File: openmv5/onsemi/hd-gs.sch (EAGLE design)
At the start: 58 parts, among them IC1 AP0202AT2L00XPGA0, IC2 MIC5365-2.8YC5-TR, IC3 TLV62568PDDCR, J1 DF12-36-DS, J2 DF12-36-DP, M1 9774030151R, M2 9774030151R, Q1 PMXB120EPEZ

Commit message: Add more cameras
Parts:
- removed J2: DF12-36-DP, DF12NB(3.0)-36DP-0.5V(51):DF12-36-DP
- removed L7: 100, 0402:INDUCTOR_0402
- removed M1, M2: 9774030151R, 9774030151R:9774030151R
- removed R5: 100K, rcl:R-US_R0402
- removed R6: 10K, rcl:R-US_R0402
- added C30, C31, C33, C34: 4.7uF, 0402:CAP_0402
- added C32, C35, C36: 22uF, SparkFun-Capacitors:22UF-0805-6.3V-20%
- added H1: LENSMOUNT20MM, lensmount:LENSMOUNT20MM
- C1, C13: value 0.22uF -> 4.7uF; device rcl:C-EUC0201 -> 0402:CAP_0402; MPN GRM033R60J224ME15D -> JMK105BBJ475MV-F
- C12: value 6.8pF -> 0.22uF; device 0402:CAP_0402 -> rcl:C-EUC0201; MPN GRM1555C1H6R8DA01D -> GRM033R60J224ME15D
- C14, C16, C18, C19, C20, C22, C23: value 4.7uF -> 0.22uF; device 0402:CAP_0402 -> rcl:C-EUC0201; MPN JMK105BBJ475MV-F -> GRM033R60J224ME15D
- C15: value 4.7uF -> 22uF; device 0402:CAP_0402 -> SparkFun-Capacitors:22UF-0805-6.3V-20%; MPN JMK105BBJ475MV-F -> CL21A226MQQNNNE
- C17, C24, C25, C26: value 22uF -> 0.22uF; device SparkFun-Capacitors:22UF-0805-6.3V-20% -> rcl:C-EUC0201; MPN CL21A226MQQNNNE -> GRM033R60J224ME15D
- C2: value 0.22uF -> 22uF; device rcl:C-EUC0201 -> SparkFun-Capacitors:22UF-0805-6.3V-20%; MPN GRM033R60J224ME15D -> CL21A226MQQNNNE
- C21: value 4.7uF -> 6.8pF; MPN JMK105BBJ475MV-F -> GRM1555C1H6R8DA01D
- C27, C29: value 22uF -> 4.7uF; device SparkFun-Capacitors:22UF-0805-6.3V-20% -> 0402:CAP_0402; MPN CL21A226MQQNNNE -> JMK105BBJ475MV-F
- IC1: value AP0202AT2L00XPGA0 -> TLV62568PDDCR; device AP0202AT2L00XPGA0:AP0202AT2L00XPGA0 -> TLV62568PDDCR:TLV62568PDDCR; MPN AP0202AT2L00XPGA0-DR -> TLV62568PDDCR
- IC2: value MIC5365-2.8YC5-TR -> AR0144CSSC20SUKA0; device MIC5365-2.8YC5-TR:MIC5365-2.8YC5-TR -> AR0144CSSC20SUKA0:AR0144CSSC20SUKA0; MPN MIC5365-2.8YC5-TR -> AR0144CSSC20SUKA0-CRBR
- IC3: value TLV62568PDDCR -> MIC5365-2.8YC5-TR; device TLV62568PDDCR:TLV62568PDDCR -> MIC5365-2.8YC5-TR:MIC5365-2.8YC5-TR; MPN TLV62568PDDCR -> MIC5365-2.8YC5-TR
- J1: value DF12-36-DS -> DF12-36-DP; device DF12-36-DS:DF12-36-DS -> DF12NB(3.0)-36DP-0.5V(51):DF12-36-DP; MPN DF12NB-36DS-0.5V(51) -> DF12NB(3.0)-36DP-0.5V(51)
- L1: value MAKK2016T2R2M -> 100; device MAKK2016T2R2M:MAKK2016T2R2M -> 0402:INDUCTOR_0402; MPN MAKK2016T2R2M -> MFBM1V1005-101-R
- L3: value 100 -> MAKK2016T2R2M; device 0402:INDUCTOR_0402 -> MAKK2016T2R2M:MAKK2016T2R2M; MPN MFBM1V1005-101-R -> MAKK2016T2R2M
- R1, R2: value 1.5K -> 100K; MPN RC0402FR-131K5L -> AC0402FR-07100KL
- R3: value 100K -> 10K; MPN AC0402FR-07100KL -> AC0402FR-1310KL
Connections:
- net SENSOR_D12 renamed DCMI_D12
- net SENSOS_D13 renamed DCMI_D13
- removed net DCMI_MISO: J1.15, J2.15
- removed net DCMI_MOSI: J1.17, J2.17
- removed net DCMI_SCLK: J1.13, J2.13
- removed net DCMI_SSEL: J1.11, J2.11
- removed net SENSOR_CLK: IC1.EXT_CLK_OUT, J1.12
- removed net SENSOR_D0: IC1.DIN_0, J1.3
- removed net SENSOR_D1: IC1.DIN_1, J1.1
- removed net SENSOR_D10: IC1.DIN_10, J1.24
- removed net SENSOR_D11: IC1.DIN_11, J1.22
- removed net SENSOR_D2: IC1.DIN_2, J1.9
- removed net SENSOR_D3: IC1.DIN_3, J1.7
- removed net SENSOR_D4: IC1.DIN_4, J1.31
- removed net SENSOR_D5: IC1.DIN_5, J1.29
- removed net SENSOR_D6: IC1.DIN_6, J1.35
- removed net SENSOR_D7: IC1.DIN_7, J1.28
- removed net SENSOR_D8: IC1.DIN_8, J1.26
- removed net SENSOR_D9: IC1.DIN_9, J1.33
- removed net SENSOR_FSIN: IC1.TRIGGER_OUT/GPIO_0, J1.23
- removed net SENSOR_HSYNC: IC1.LV_IN, J1.18
- removed net SENSOR_PCLK: IC1.PIXCLK_IN, J1.14
- removed net SENSOR_RST: IC1.RESET_N_OUT, J1.21
- removed net SENSOR_SCL: IC1.M_SCLK, J1.32, R1.1
- removed net SENSOR_SDA: IC1.M_SDATA, J1.34, R2.1
- removed net SENSOR_VSYNC: IC1.FV_IN, J1.16
- removed net VDDIO_H: C13.2, C19.2, C2.2, C25.2, C3.2, C4.2, IC1.EXT_REG, IC1.SADDR, IC1.VDDIO_H0, IC1.VDDIO_H1, IC1.VDDIO_H2, IC1.VDD_REG, L3.P$1
- removed net VDDIO_OTPM: C10.2, C18.2, C24.2, IC1.VDDIO_OTPM, L2.P$1
- removed net VDDIO_S: C1.2, C20.2, C26.2, IC1.VDDIO_S, L4.P$1
- removed net VDD_PLL: C22.2, C28.2, C5.2, IC1.VDD_PLL, L6.P$1
- new net DCMI_D10: IC2.DOUT10, J1.24
- new net DCMI_D11: IC2.DOUT11, J1.22
- new net DCMI_D8: IC2.DOUT8, J1.26
- new net DCMI_D9: IC2.DOUT9, J1.33
- new net SPI_MISO: J1.15
- new net SPI_MOSI: J1.17
- new net SPI_SCLK: J1.13
- new net SPI_SSEL: J1.11
- new net VAA: C3.1, C31.2, C32.2, C4.1, C5.1, C6.1, C7.1, C8.1, IC2.VAA0, IC2.VAA1, IC2.VAA2, IC2.VAA3, IC2.VAA4, IC2.VAA5, L4.P$1
- new net VAA_PIX: C20.1, C33.2, C35.2, IC2.VAA_PIX, L5.P$1
- new net VDDIO: C22.1, C23.1, C24.1, C25.1, C26.1, C34.2, C36.2, IC2.VDDIO0, IC2.VDDIO1, IC2.VDDIO2, IC2.VDDIO3, IC2.VDDIO4, L6.P$1
- net DCMI_CLK: now also IC2.EXTCLK, J1.12; no longer IC1.EXTCLK, J2.12
- net DCMI_D0: now also IC2.DOUT0, J1.3; no longer IC1.DOUT_16, J2.31
- net DCMI_D1: now also IC2.DOUT1, J1.1; no longer IC1.DOUT_17, J2.29
- net DCMI_D2: now also IC2.DOUT2, J1.9; no longer IC1.DOUT_18, J2.35
- net DCMI_D3: now also IC2.DOUT3, J1.7; no longer IC1.DOUT_19, J2.28
- net DCMI_D4: now also IC2.DOUT4, J1.31; no longer IC1.DOUT_20, J2.26
- net DCMI_D5: now also IC2.DOUT5, J1.29; no longer IC1.DOUT_21, J2.33
- net DCMI_D6: now also IC2.DOUT6, J1.35; no longer IC1.DOUT_22, J2.24
- net DCMI_D7: now also IC2.DOUT7, J1.28; no longer IC1.DOUT_23, J2.22
- net DCMI_FSIN: now also IC2.TRIGGER, J1.23; no longer IC1.FRAME_SYNC, J2.23
- net DCMI_HSYNC: now also IC2.LINE_VALID, J1.18; no longer IC1.LV_OUT, J2.18
- net DCMI_PCLK: now also IC2.PIXCLK, J1.14; no longer IC1.PIXCLK_OUT, J2.14
- net DCMI_PWDN: no longer IC1.STANDBY, J2.25
- net DCMI_PWDN_INT: now also IC3.EN, R4.1; no longer IC2.EN, R5.1
- net DCMI_RST: now also J1.21, R3.2; no longer J2.21, R6.2
- net DCMI_SCL: now also IC2.SCLK, J1.32; no longer IC1.SCLK, J2.32
- net DCMI_SDA: now also IC2.SDATA, J1.34; no longer IC1.SDATA, J2.34
- net DCMI_VSYNC: now also IC2.FRAME_VALID, J1.16; no longer IC1.FV_OUT, J2.16
- net FB: now also C21.2, IC1.FB, R1.1, R2.1; no longer C12.2, IC3.FB, R3.1, R4.1
- net GND: now also C10.2, C11.2, C12.2, C14.2, C16.2, C17.2, C18.2, C19.2, C20.2, C22.2, C23.2, C24.2, C25.2, C26.2, C3.2, C30.1, C31.1, C32.1, C33.1, C34.1, C35.1, C36.1, C4.2, C5.2, C6.2, C7.2, C8.2, C9.2, IC1.GND, IC2.AGND0, IC2.AGND1, IC2.AGND2, IC2.AGND3, IC2.AGND4, IC2.DGND0, IC2.DGND1, IC2.DGND2, IC2.DGND3, IC2.DGND4, IC2.DGND5, IC2.DGND6, IC2.DGND7, IC2.DGND8, IC2.DGND9, IC2.OE_N, IC2.SADDR, IC2.TEST, R2.2; no longer C10.1, C11.1, C14.1, C16.1, C17.1, C18.1, C19.1, C20.1, C21.1, C22.1, C23.1, C24.1, C25.1, C26.1, C3.1, C4.1, C5.1, C6.1, C7.1, C8.1, C9.1, IC1.DGND, IC1.ENDLO, IC1.GND0, IC1.GND1, IC1.GND2, IC1.GND3, IC1.GND4, IC1.GND5, IC1.GND6, IC1.GND7, IC1.HISPI0N, IC1.HISPI0P, IC1.HISPI1N, IC1.HISPI1P, IC1.HISPICN, IC1.HISPICP, IC1.RESERVED_0, IC1.RESERVED_1, IC1.SPI_SDI, IC1.TEST, IC2.GND, J2.19, J2.27, J2.5, R5.2
- net RESET_N: now also IC1.PG, IC2.RESET_N, R3.1; no longer IC1.RESET_N, IC3.PG, R6.1
- net SW: now also IC1.SW, L3.2; no longer IC3.SW, L1.2
- net VCC: now also C27.2, IC1.VIN; no longer C15.2, C16.2, IC2.VIN, IC3.VIN, J2.10, J2.2, J2.20, J2.30, J2.36, L2.P$2, L3.P$2, Q1.S, R1.2, R2.2
- net VDD: now also C1.2, C10.1, C11.1, C12.1, C14.1, C16.1, C17.1, C18.1, C19.1, C2.2, IC2.VDD0, IC2.VDD1, IC2.VDD2, IC2.VDD3, IC2.VDD4, IC2.VDD5, IC2.VDD6, IC2.VDD7, L1.P$1; no longer C23.2, C29.2, C6.2, C7.2, C8.2, C9.2, IC1.VDD0, IC1.VDD1, IC1.VDD2, IC1.VDD3, L7.P$1
- net VDDA: now also C30.2, IC3.VIN, Q1.S; no longer J2.4
- net VDDIO_REG: now also C29.2, IC1.EN, IC3.VOUT, L6.P$2; no longer C14.2, IC2.VOUT, IC3.EN
- net VDD_PHY: now also C13.2, C15.2, C9.1, IC2.VDD_PHY, L2.P$1; no longer C11.2, C21.2, C27.2, IC1.VDD_PHY, L5.P$1
- net VDD_REG: now also C21.1, C28.2, L1.P$2, L2.P$2, L3.1, R1.2; no longer C12.1, C17.2, L1.1, L6.P$2, L7.P$2, R3.2
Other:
- note added: "Camera Sensor"
- note added: "Connector"
- note removed: "Host Connector"
- note removed: "ISP"
- note removed: "SENSOR CONNECTOR"
- moved on the sheet: C1, C10, C11, C12, C13, C14, C15, C16, C17, C18, C19, C2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

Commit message: Finish out new onsemi cameras
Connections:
- removed net DCMI_D12: J1.8
- removed net DCMI_D13: J1.6
- net GND: now also J1.6, J1.8
- net SPI_MISO: now also IC2.FLASH
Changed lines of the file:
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@@
 <wire x1="17.78" y1="220.98" x2="43.18" y2="220.98" width="0.1524" layer="91"/>
+</segment>
+<segment>
+<wire x1="381" y1="228.6" x2="411.48" y2="228.6" width="0.1524" layer="91"/>
+<label x="386.08" y="228.6" size="1.778" layer="95"/>
+<pinref part="J1" gate="G$1" pin="6"/>
+</segment>
+<segment>
+<wire x1="381" y1="226.06" x2="411.48" y2="226.06" width="0.1524" layer="91"/>
+<label x="386.08" y="226.06" size="1.778" layer="95"/>
+<pinref part="J1" gate="G$1" pin="8"/>
 </segment>
 </net>
@@
 <pinref part="J1" gate="G$1" pin="15"/>
 </segment>
+<segment>
+<pinref part="IC2" gate="G$1" pin="FLASH"/>
+<wire x1="43.18" y1="200.66" x2="22.86" y2="200.66" width="0.1524" layer="91"/>
+<label x="25.4" y="200.66" size="1.778" layer="95"/>
+</segment>
 </net>
 <net name="SPI_MOSI" class="4">
@@
 </segment>
 </net>
-<net name="DCMI_D13" class="4">
-<segment>
-<wire x1="381" y1="228.6" x2="411.48" y2="228.6" width="0.1524" layer="91"/>
-<label x="386.08" y="228.6" size="1.778" layer="95"/>
-<pinref part="J1" gate="G$1" pin="6"/>
-</segment>
-</net>
-<net name="DCMI_D12" class="4">
-<segment>
-<wire x1="381" y1="226.06" x2="411.48" y2="226.06" width="0.1524" layer="91"/>
-<label x="386.08" y="226.06" size="1.778" layer="95"/>
-<pinref part="J1" gate="G$1" pin="8"/>
-</segment>
-</net>

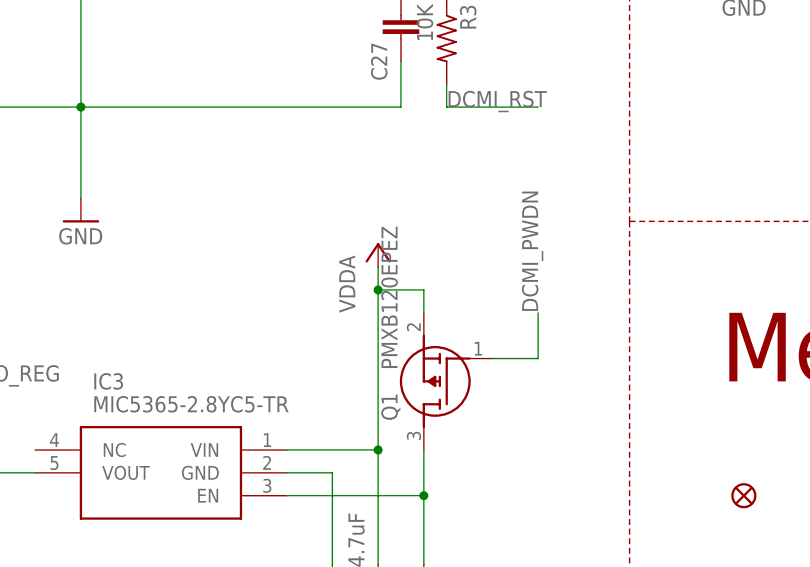
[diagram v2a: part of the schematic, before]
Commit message: Update camera modules to use different non-flippable pmosfet
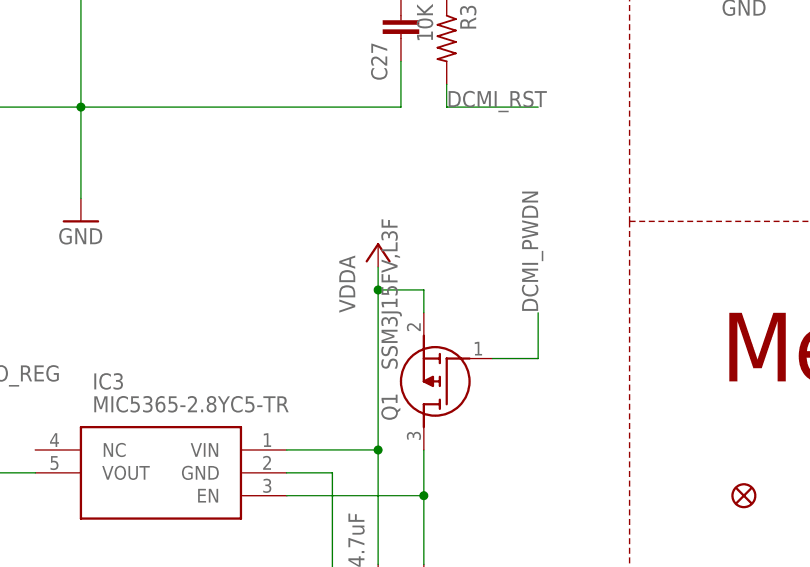
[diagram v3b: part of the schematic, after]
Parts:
- Q1: value PMXB120EPEZ -> SSM3J15FV,L3F; device PMXB120EPEZ:PMXB120EPEZ -> SSM3J15FV_L3F:SSM3J15FV,L3F; MPN PMXB120EPEZ -> SSM3J15FV,L3F
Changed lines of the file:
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@@
 </part>
 <part name="GND11" library="supply" deviceset="GND" device=""/>
-<part name="Q1" library="PMXB120EPEZ" deviceset="PMXB120EPEZ" device="">
-<attribute name="MPN" value="PMXB120EPEZ"/>
+<part name="Q1" library="SSM3J15FV_L3F" deviceset="SSM3J15FV,L3F" device="">
+<attribute name="MPN" value="SSM3J15FV,L3F"/>
 </part>
 <part name="R4" library="rcl" library_urn="urn:adsk.eagle:library:334" deviceset="R-US_" device="R0402" package3d_urn="urn:adsk.eagle:package:23547/3" value="100K">
